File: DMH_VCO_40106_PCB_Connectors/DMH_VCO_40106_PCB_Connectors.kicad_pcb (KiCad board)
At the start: 2 copper layers, 98 x 62 mm, 16 parts, among them J1 TS_Jack_6.35mm_Sw, J150 Conn_01x12, J2 TS_Jack_6.35mm_Sw, J200 IDC_02x05, J3 TS_Jack_6.35mm_Sw, J4 TS_Jack_6.35mm_Sw, J5 TS_Jack_6.35mm_Sw, J6 TS_Jack_6.35mm_Sw, J7 TS_Jack_6.35mm_Sw, J8 TS_Jack_6.35mm_Sw, J9 TS_Jack_6.35mm_Sw

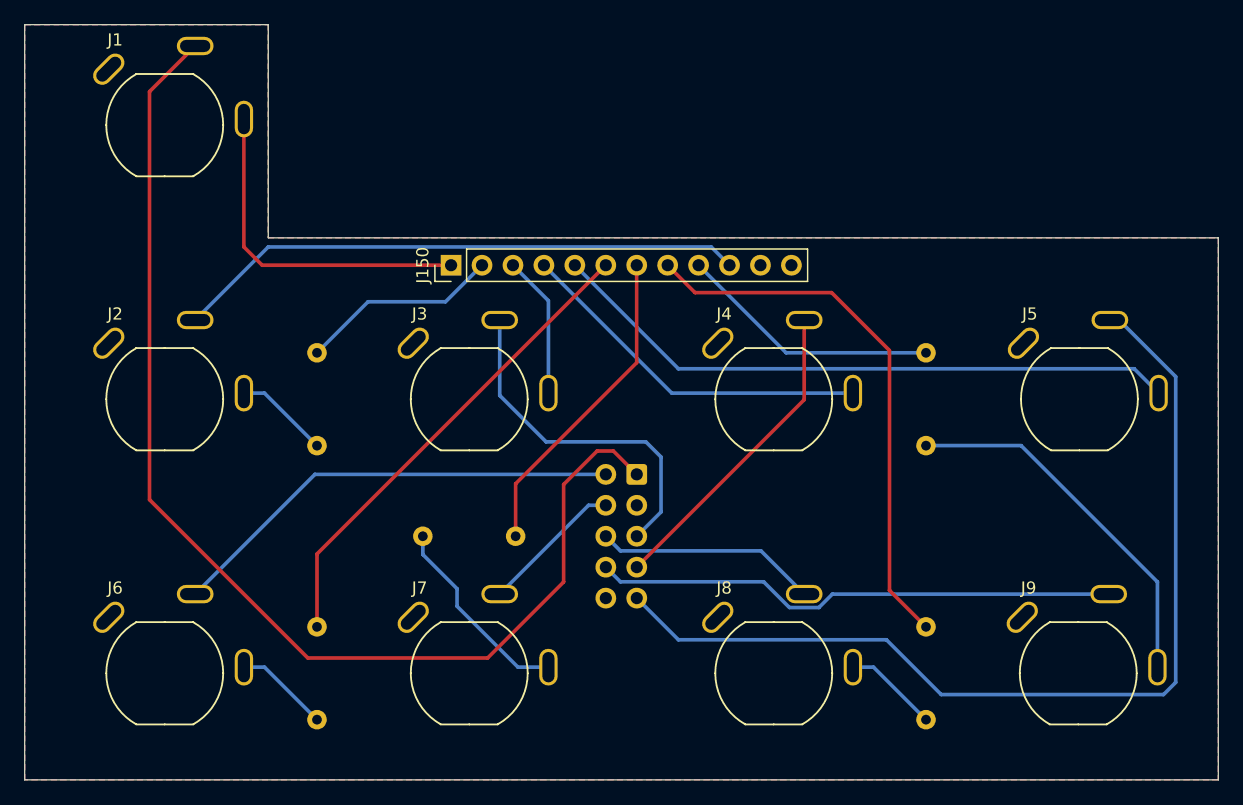
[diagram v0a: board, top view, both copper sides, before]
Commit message: Placed input and output resistors back in main PCB
This ensures a more clear schematic and leaves the Connectors PCB only with actual connectors.
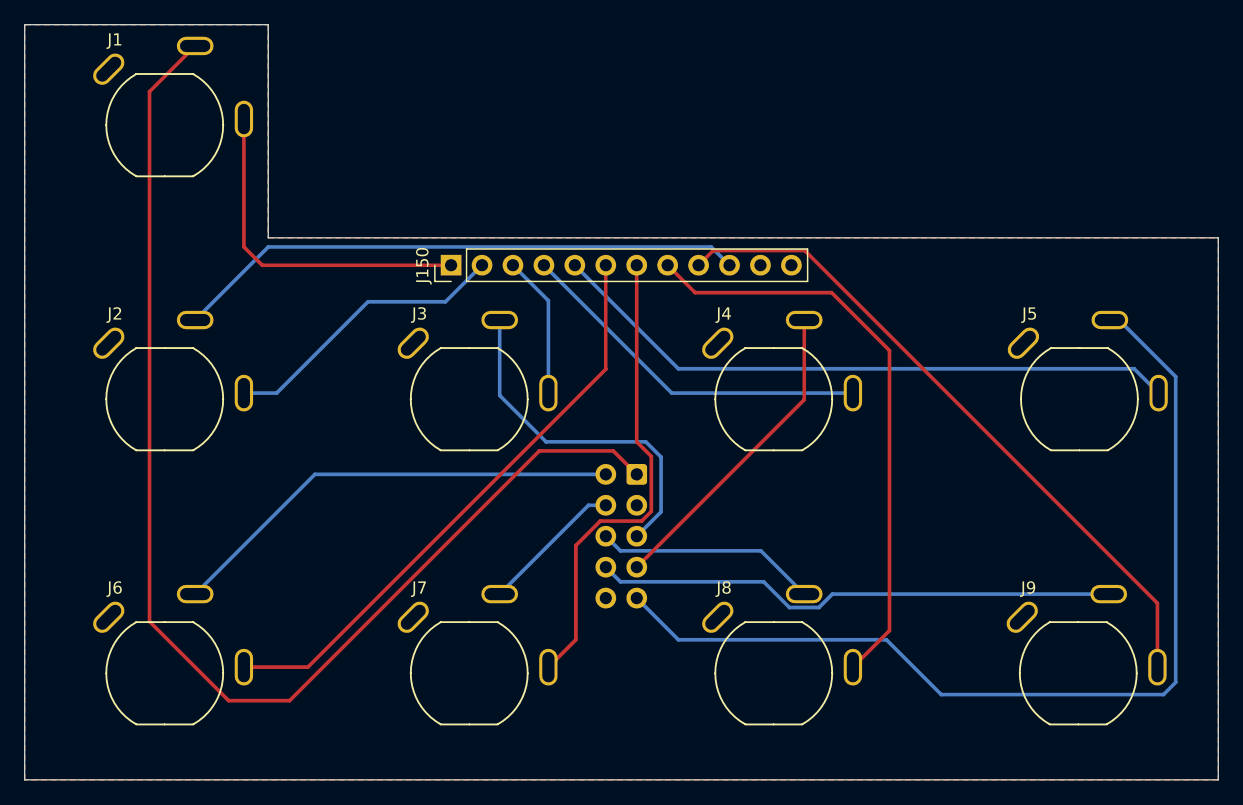
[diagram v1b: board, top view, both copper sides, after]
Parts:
- removed R20, R21, R28, R44: 1k, Resistor_THT:R_Axial_DIN0207_L6.3mm_D2.5mm_P7.62mm_Horizontal
- removed R7: 100k, Resistor_THT:R_Axial_DIN0207_L6.3mm_D2.5mm_P7.62mm_Horizontal
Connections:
- J2 pad T: Net-(J2-PadT) -> Net-(J150-Pin_2)
- J6 pad T: Net-(J6-PadT) -> Net-(J150-Pin_6)
- J7 pad T: Net-(J7-PadT) -> Net-(J150-Pin_7)
- J8 pad T: Net-(J8-PadT) -> Net-(J150-Pin_8)
- J9 pad T: Net-(J9-PadT) -> Net-(J150-Pin_9)
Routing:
- net Net-(J150-Pin_9): track 21.6 -> 55.4 mm
- net Net-(J9-PadT): track 30.6 -> 0.00 mm
- net Net-(J7-PadT): track 16.5 -> 0.00 mm
- net Net-(J150-Pin_7): track 26.4 -> 39.0 mm
- net Net-(J150-Pin_6): track 39.5 -> 48.4 mm
- net Net-(J8-PadT): track 7.79 -> 0.00 mm
- net Net-(J6-PadT): track 7.79 -> 0.00 mm
- net Net-(J2-PadT): track 7.79 -> 0.00 mm
- net Net-(J150-Pin_2): track 16.8 -> 24.2 mm
- net Net-(J200-Pin_1): track 96.7 -> 100.8 mm
- net Net-(J150-Pin_8): track 45.0 -> 48.4 mm

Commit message: Prepared PCBs for fabrication
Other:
- board text added: "Mk1.1 - September 2024"
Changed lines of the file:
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@@
 			(plot_on_all_layers_selection 0x0000000_00000000)
 			(disableapertmacros no)
-			(usegerberextensions no)
-			(usegerberattributes yes)
-			(usegerberadvancedattributes yes)
+			(usegerberextensions yes)
+			(usegerberattributes no)
+			(usegerberadvancedattributes no)
 			(creategerberjobfile yes)
 			(dashed_line_dash_ratio 12.000000)
@@
 			(plotinvisibletext no)
 			(sketchpadsonfab no)
-			(subtractmaskfromsilk no)
+			(subtractmaskfromsilk yes)
 			(outputformat 1)
 			(mirror no)
-			(drillshape 1)
+			(drillshape 0)
 			(scaleselection 1)
 			(outputdirectory "")
@@
 			)
 		)
-		(property "Function" "Exp FM"
+		(property "Function" "Exp FM 1"
 			(at 0 0 0)
 			(unlocked yes)
@@
 			)
 		)
-		(property "Function" "Exp FM"
+		(property "Function" "Exp FM 2"
 			(at 0 0 0)
 			(unlocked yes)
@@
 	)
 	(gr_text "JLCJLCJLCJLC"
-		(at 100 236 0)
+		(at 142.75 236.25 0)
 		(layer "B.SilkS")
 		(effects
@@
 			)
 			(justify mirror)
+		)
+	)
+	(gr_text "Mk1.1 - September 2024"
+		(at 138.25 234.25 0)
+		(layer "B.SilkS")
+		(effects
+			(font
+				(size 1 1)
+				(thickness 0.25)
+				(bold yes)
+			)
+			(justify mirror)

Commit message: Replaced JLCJLCJLCJLC with space for serial number
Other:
- board text removed: "JLCJLCJLCJLC"
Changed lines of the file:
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@@
 		)
+	)
+	(gr_rect
+		(start 116 234.5)
+		(end 126 236.5)
+		(stroke
+			(width 0.1)
+			(type solid)
+		)
+		(fill solid)
+		(layer "B.SilkS")
 	)
 	(gr_circle
@@
 		(layer "User.9")
 	)
-	(gr_text "JLCJLCJLCJLC"
-		(at 142.75 236.25 0)
+	(gr_text "Mk1.1 - September 2024"
+		(at 138.25 235.5 0)
 		(layer "B.SilkS")
 		(effects
-			(font
-				(size 1 1)
-				(thickness 0.15)
-			)
-			(justify mirror)
-		)
-	)
-	(gr_text "Mk1.1 - September 2024"
-		(at 138.25 234.25 0)
-		(layer "B.SilkS")
-		(effects
